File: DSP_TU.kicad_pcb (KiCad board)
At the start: 4 copper layers, 158 x 79 mm, 72 parts, among them J1 Conn_01x07_Male, J2 Conn_01x08_Male, J3 USB_B, J5 1757569, K1 G3VM-601BY, K2 G3VM-601BY, T1 TY-141P, T2 TY-145P, U1 PIC32MZ0512EFE064-I_PT, U2 TLV2780CDBVT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

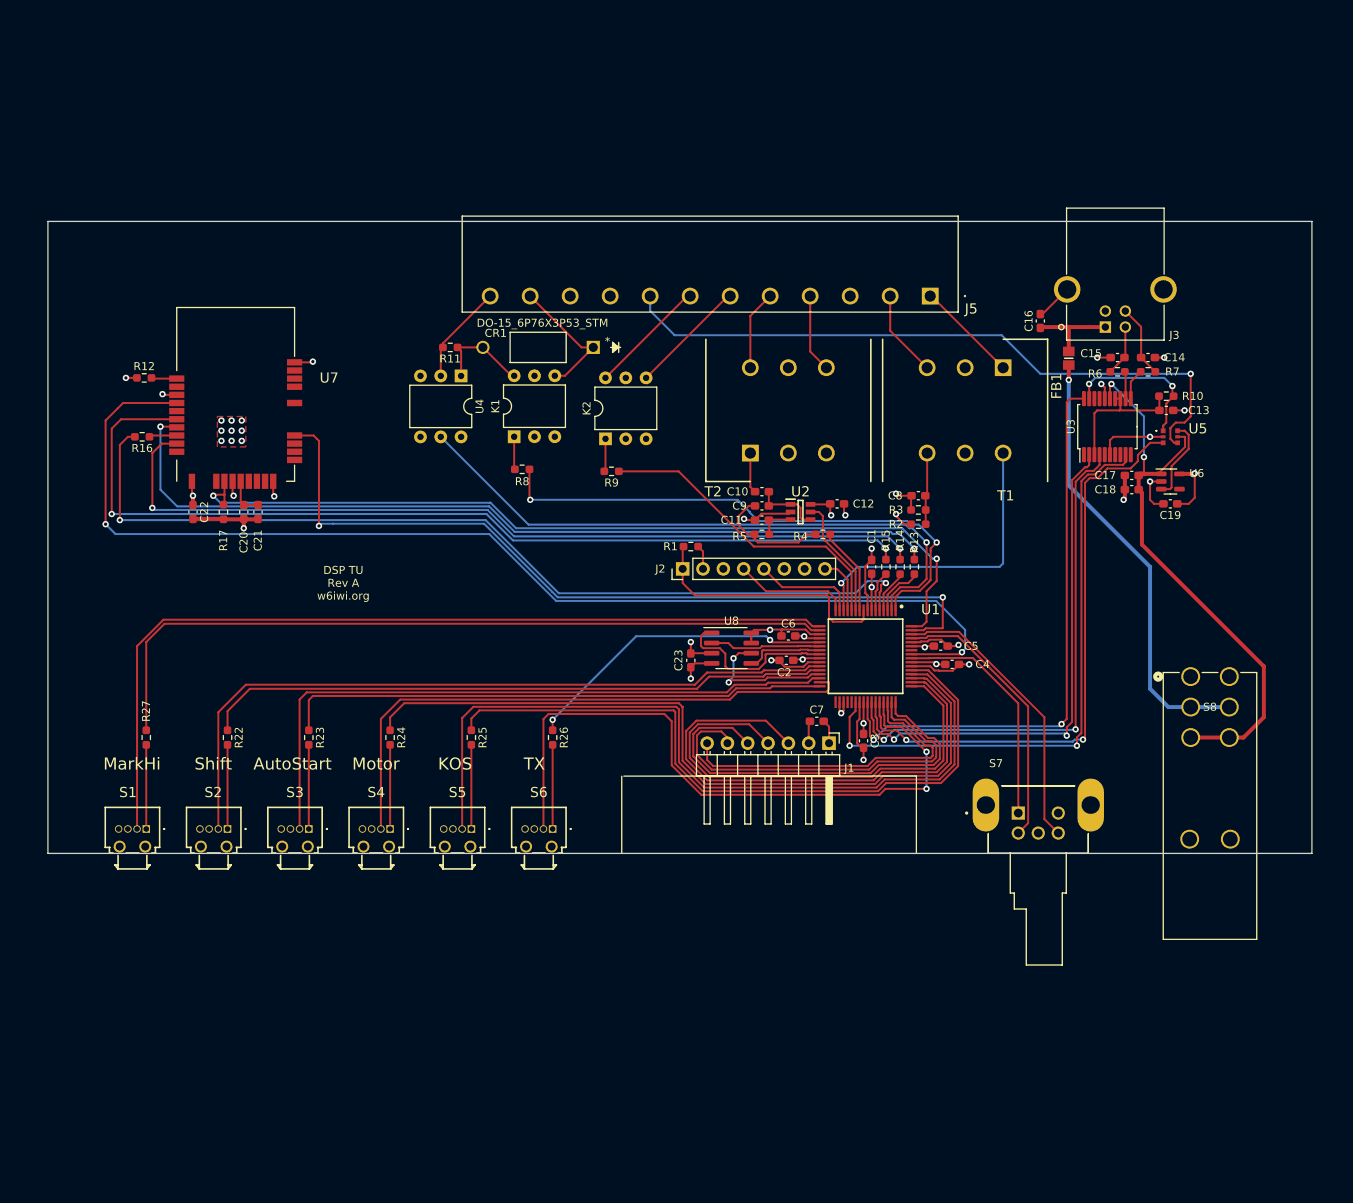
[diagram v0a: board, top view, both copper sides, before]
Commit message: PCB Rev B, changing dimensions, adding test points, adding resistors in UART lines, and correcting display pinout. hh
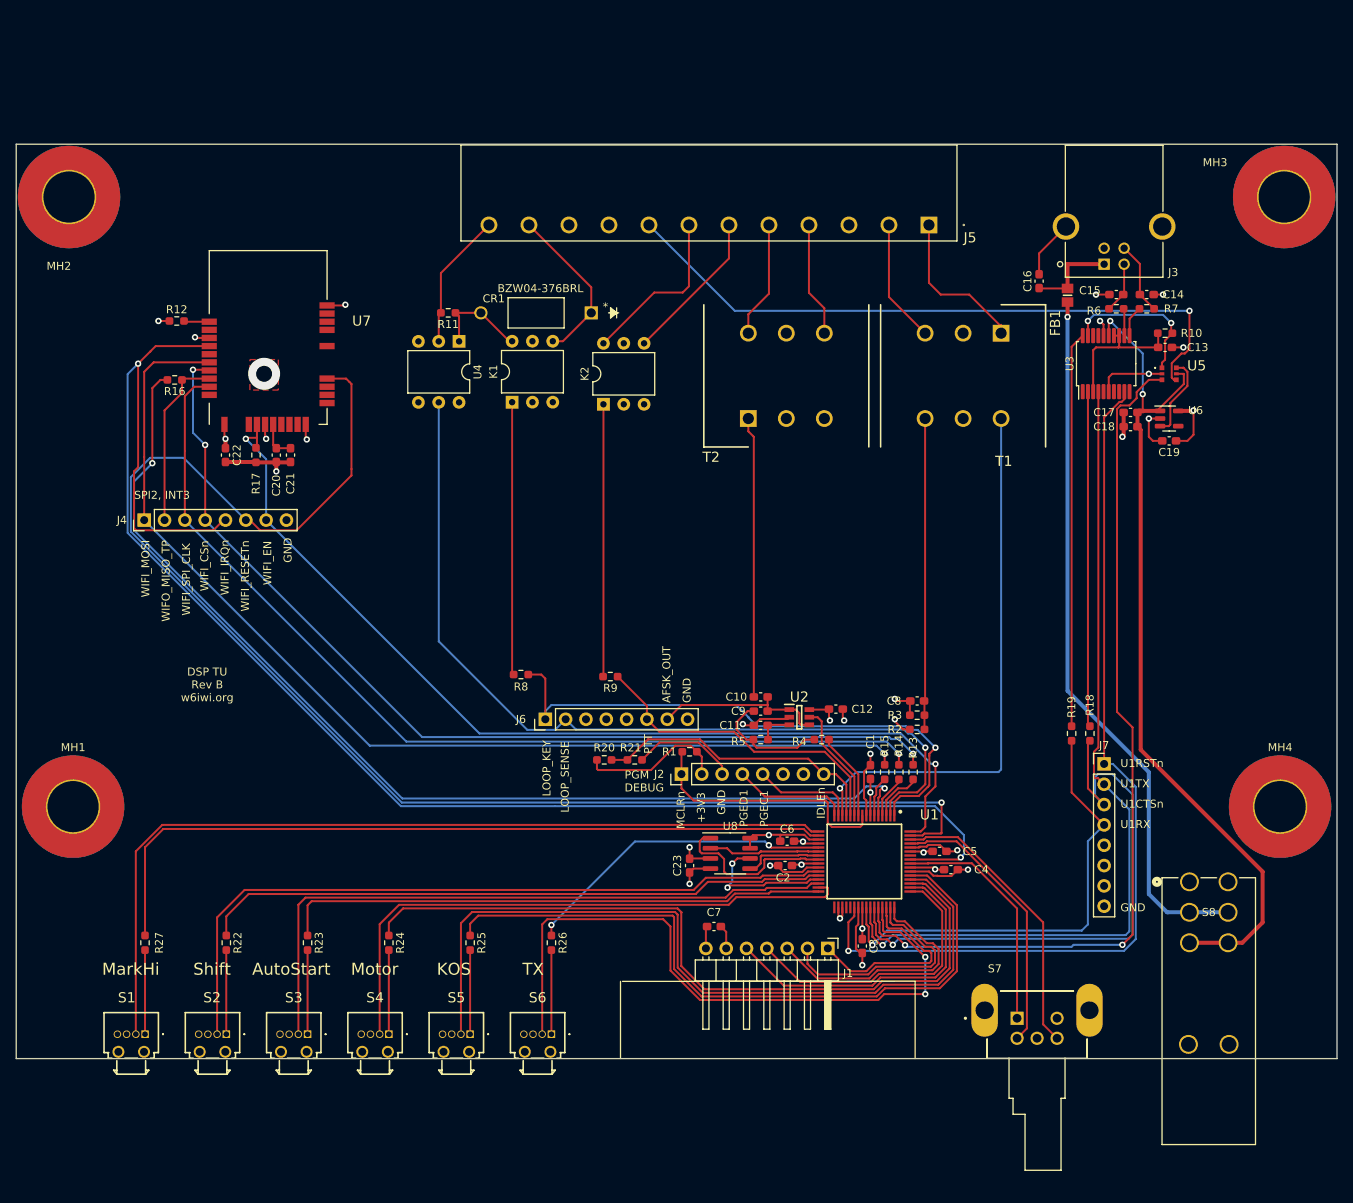
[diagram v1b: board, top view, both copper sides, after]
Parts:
- added J4: Conn_01x08_Male, Connector_PinHeader_2.54mm:PinHeader_1x08_P2.54mm_Vertical, F.Cu at (50.0, 76.2)
- added J6: Conn_01x08_Male, Connector_PinHeader_2.54mm:PinHeader_1x08_P2.54mm_Vertical, F.Cu at (100.2, 101.1)
- added J7: Conn_01x08_Male, Connector_PinHeader_2.54mm:PinHeader_1x08_P2.54mm_Vertical, F.Cu at (170.0, 106.7)
- added MH1: MountingHole_6.4mm_M6_Pad_TopBottom, MountingHole:MountingHole_6.4mm_M6_Pad_TopBottom, F.Cu at (41.1, 112.0)
- added MH2: MountingHole_6.4mm_M6_Pad_TopBottom, MountingHole:MountingHole_6.4mm_M6_Pad_TopBottom, F.Cu at (40.6, 35.8)
- added MH3: MountingHole_6.4mm_M6_Pad_TopBottom, MountingHole:MountingHole_6.4mm_M6_Pad_TopBottom, F.Cu at (192.5, 35.8)
- added MH4: MountingHole_6.4mm_M6_Pad_TopBottom, MountingHole:MountingHole_6.4mm_M6_Pad_TopBottom, F.Cu at (192.0, 112.0)
- added R18: 1k, Resistor_SMD:R_0603_1608Metric_Pad0.98x0.95mm_HandSolder, F.Cu at (168.2, 102.9)
- added R19: 1k, Resistor_SMD:R_0603_1608Metric_Pad0.98x0.95mm_HandSolder, F.Cu at (166.0, 102.9)
- added R20: 10k, Resistor_SMD:R_0603_1608Metric_Pad0.98x0.95mm_HandSolder, F.Cu at (107.5, 106.2)
- added R21: 1k, Resistor_SMD:R_0603_1608Metric_Pad0.98x0.95mm_HandSolder, F.Cu at (111.4, 106.2)
- CR1: value DO-15_6P76X3P53_STM -> BZW04-376BRL
- moved C7 28.7 mm to (121.3, 127.0), turned to 180 degrees
- moved C3 25.7 mm to (139.8, 129.4)
- moved C4 25.7 mm to (150.9, 119.9)
- moved C5 25.7 mm to (149.5, 117.6)
- moved R1 25.7 mm to (118.2, 105.2)
- moved R22 25.7 mm to (60.3, 129.0)
- moved R23 25.7 mm to (70.5, 129.0)
- moved R24 25.7 mm to (80.6, 129.0)
- moved R25 25.7 mm to (90.8, 129.0)
- moved R26 25.7 mm to (100.9, 129.0)
- moved R27 25.7 mm to (50.1, 129.0)
- moved R4 25.7 mm to (134.7, 103.6)
- moved R5 25.7 mm to (127.1, 103.6)
- moved R8 25.7 mm to (97.1, 95.5)
- moved S8 25.7 mm to (180.7, 121.4)
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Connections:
- net AFSK_OUT_ENn renamed AFSK_OUT_EN
- net Net-(C10-Pad2) renamed AFSK_OUT
- net Net-(R16-Pad1) renamed WIFI_MISO_TP
- J1 pad 1: +3V3 -> Net-(J1-Pin_1)
- J1 pad 2: GND -> Net-(J1-Pin_2)
- J1 pad 3: Net-(J1-Pad3) -> Net-(J1-Pin_3)
- J1 pad 5: Net-(J1-Pad5) -> Net-(J1-Pin_5)
- J1 pad 6: Net-(J1-Pad6) -> GND
- J1 pad 7: Net-(J1-Pad7) -> +3V3
- U1 pad 46: Net-(J1-Pad7) -> Net-(J1-Pin_1)
- U1 pad 47: Net-(J1-Pad6) -> Net-(J1-Pin_2)
- U1 pad 48: Net-(J1-Pad5) -> Net-(J1-Pin_3)
- U1 pad 50: Net-(J1-Pad3) -> Net-(J1-Pin_5)
- U3 pad 2: U1CTSn -> Net-(U3-RTS#)
- U3 pad 20: U1RX -> Net-(U3-TXD)
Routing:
- net WIFI_RESETn: track 103.7 -> 180.0 mm, vias 2 -> 1
- net Net-(J1-Pad3): track 65.5 -> 0.00 mm
- net Net-(J1-Pad5): track 53.5 -> 0.00 mm
- net Net-(U3-TXD): track 0.00 -> 49.4 mm
- net Net-(J1-Pad6): track 49.2 -> 0.00 mm
- net WIFI_IRQn: track 145.0 -> 193.9 mm
- net Net-(U3-RTS#): track 0.00 -> 41.9 mm
- net Net-(J1-Pad7): track 41.5 -> 0.00 mm
- net U1TX: track 66.1 -> 106.9 mm, vias 2 -> 1
- net Net-(J1-Pin_5): track 0.00 -> 40.6 mm
- net U1RTSn: track 74.9 -> 114.2 mm, vias 2 -> 1
- net AUTOSTARTn: track 73.8 -> 110.3 mm
- net +5V_SW: track 71.7 -> 105.2 mm
- net +5V: track 55.5 -> 89.1 mm
- net Net-(J1-Pin_3): track 0.00 -> 31.6 mm
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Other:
- board size 158 x 79 mm -> 165.1 x 114.3 mm
- board text added: "+3V3"
- board text added: "AFSK_OUT"
- board text added: "DSP TU Rev B w6iwi.org"
- board text added: "GND"
- board text added: "IDLEn"
- board text added: "LOOP_KEY"
- board text added: "LOOP_SENSE"
- board text added: "MCLRn"
- board text added: "PGEC1"
- board text added: "PGED1"
- board text added: "PGM DEBUG"
- board text added: "PTT"
- board text added: "SPI2, INT3"
- board text added: "U1CTSn"
- board text added: "U1RSTn"
- board text added: "U1RX"
- board text added: "U1TX"
- board text added: "WIFI_CSn"
- board text added: "WIFI_EN"
- board text added: "WIFI_IRQn"
- board text added: "WIFI_MOSI"
- board text added: "WIFI_RESETn"
- board text added: "WIFI_SPI_CLK"
- board text added: "WIFO_MISO_TP"
- board text removed: "DSP TU Rev A w6iwi.org"

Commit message: Update all to rev C
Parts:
- removed MH4: MountingHole_6.4mm_M6_Pad_TopBottom, MountingHole:MountingHole_6.4mm_M6_Pad_TopBottom
- MH1, MH2, MH3: value MountingHole_6.4mm_M6_Pad_TopBottom -> MountingHole_4.5mm; footprint MountingHole:MountingHole_6.4mm_M6_Pad_TopBottom -> MountingHole:MountingHole_4.5mm
- moved MH2 79.8 mm to (116.6, 60.5)
- moved MH3 64.4 mm to (176.6, 98.3)
- moved MH1 20.7 mm to (56.6, 98.3)
- moved K2 16.7 mm to (110.5, 45.3)
- moved R11 16.7 mm to (91.1, 33.9)
- moved CR1 16.7 mm to (109.0, 33.9)
- moved K1 16.7 mm to (99.1, 45.1)
- moved U4 16.7 mm to (92.4, 37.5)
- moved T1 16.3 mm to (155.8, 36.6)
- moved T2 16.3 mm to (124.2, 47.2)
- moved J5 15.9 mm to (148.1, 23.4)
- moved C16 15.8 mm to (161.9, 30.5)
- moved J3 15.5 mm to (170.0, 28.7)
- moved C18 13.2 mm to (173.3, 51.3)
- moved C13 13.2 mm to (177.6, 41.4)
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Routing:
- net +5V: track 89.1 -> 117.6 mm, vias 1 -> 0
- net Net-(K1-Pad1): track 34.1 -> 51.9 mm
- net Net-(K2-Pad1): track 34.1 -> 51.8 mm
- net Net-(T1-SEC_1): track 39.3 -> 56.2 mm
- net Net-(C10-Pad1): track 35.1 -> 51.9 mm
- net LOOP_SENSE: track 108.9 -> 124.1 mm
- net +5V_SW: track 105.2 -> 119.4 mm
- net U1RTSn: track 114.2 -> 127.4 mm
- net U1TX: track 106.9 -> 120.1 mm
- net Net-(U3-TXD): track 49.4 -> 62.6 mm
- net Net-(U3-RTS#): track 41.9 -> 55.2 mm
- net AUTOSTARTn: track 110.3 -> 123.5 mm
- net Net-(T1-SEC_3): track 68.5 -> 79.5 mm
- net AUTOSTART: track 82.2 -> 92.0 mm
- net PTTb: track 21.3 -> 18.1 mm
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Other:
- board size 165.1 x 114.3 mm -> 159 x 132.3 mm
- board text added: "DSP TU Rev C w6iwi.org"
- board text removed: "DSP TU Rev B w6iwi.org"
